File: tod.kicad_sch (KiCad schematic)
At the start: 65 parts, among them J1 2xMVE252, J2 MV133, J3 2xMVE252, J4 MV133, Q1 BC856B, Q2 BC817, Q3 BC856B, Q4 BC817, Q5 BC856, Q6 BC817, Q7 BC856, Q8 BC817, U1 PC817, U2 PC817, U3 PC817, U4 PC817

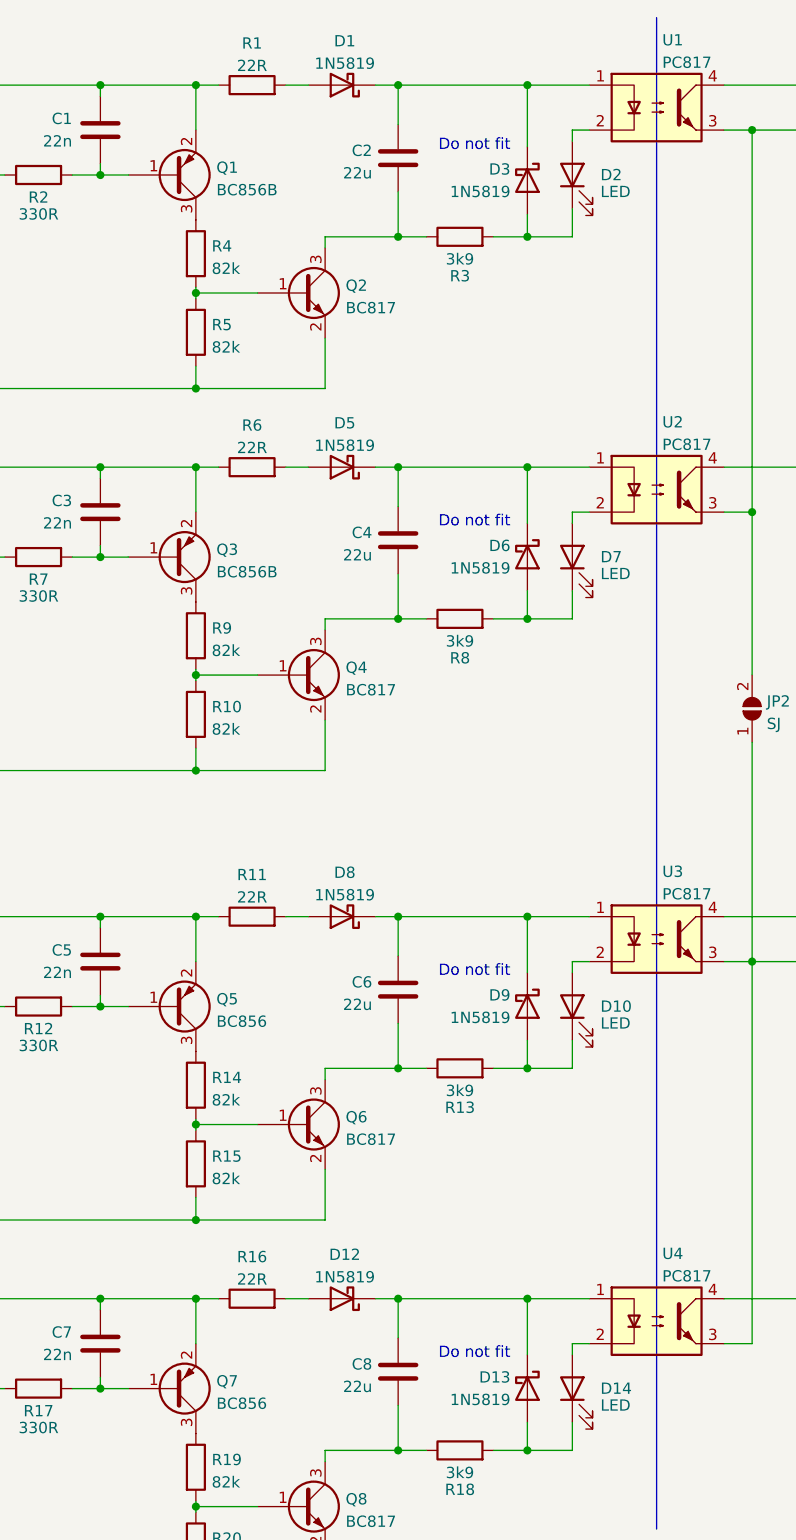
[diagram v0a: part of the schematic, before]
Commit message: Use electrolytic capacitors for 22uF C.
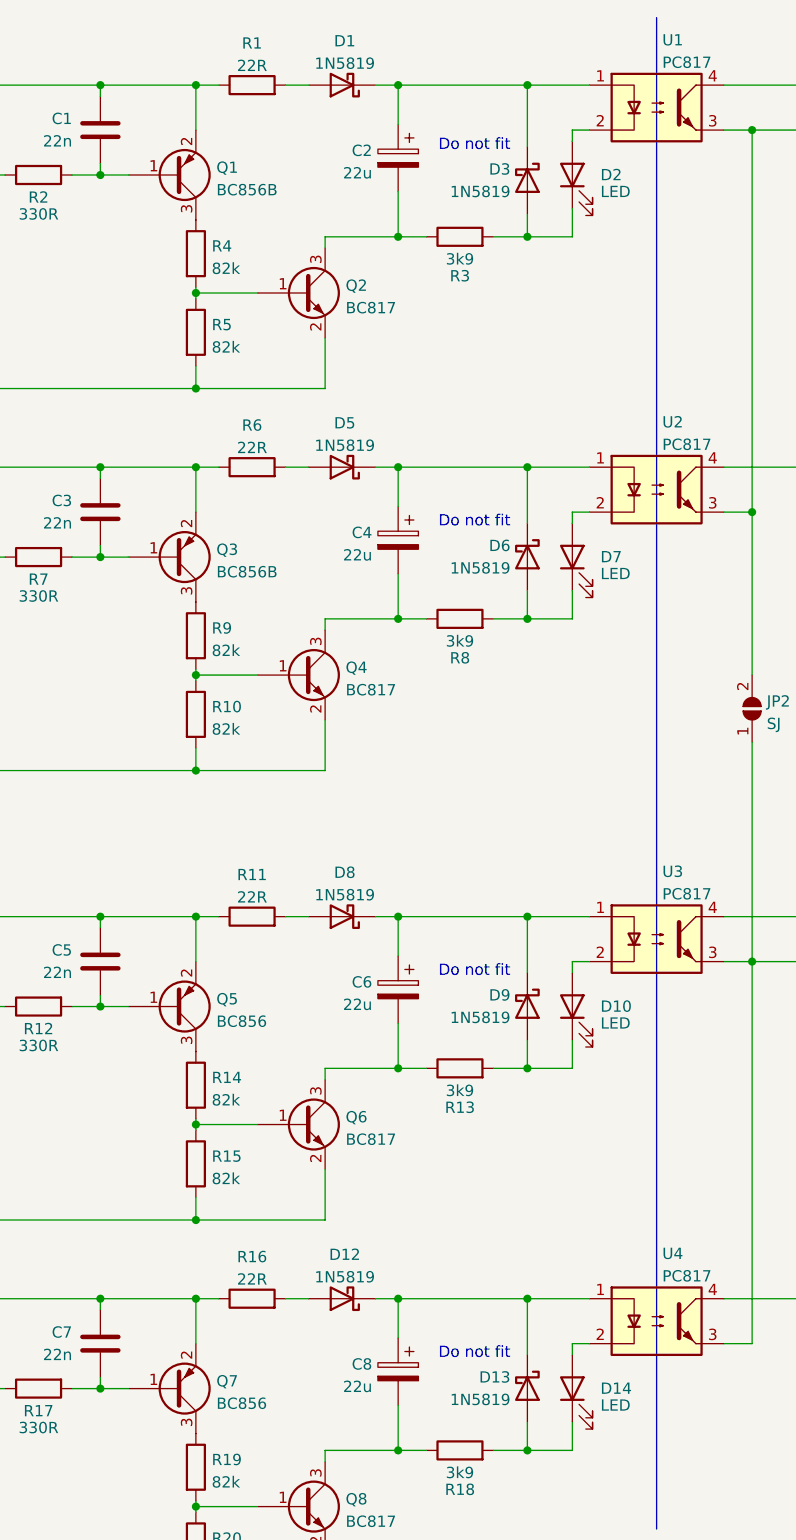
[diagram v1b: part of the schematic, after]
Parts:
- C2, C4, C6, C8: footprint Capacitor_SMD:C_0805_2012Metric_Pad1.18x1.45mm_HandSolder -> Capacitor_THT:CP_Radial_D5.0mm_P2.00mm; symbol Device:C -> Device:C_Polarized
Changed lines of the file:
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@@
   (title_block
     (title "DCC Track Occupancy Detector")
-    (date "2023-03-15")
-    (rev "1.2")
+    (date "2023-04-20")
+    (rev "1.3")
     (company "Model Railroader Club Brno I – KMŽ Brno I – https://kmz-brno.cz/")
     (comment 1 "Jan Horáček")
@@
     (pin "2")
   )
-  (symbol (lib_id "Device:C") (at 116.84 123.825 0) (mirror y) (unit 1)
+  (symbol (lib_id "Device:C_Polarized") (at 116.84 123.825 0) (mirror y) (unit 1)
     (in_bom yes) (on_board yes)
     (property "Reference" "C6" (id 0) (at 113.919 122.9903 0)
@@
       (effects (font (size 1.27 1.27)) (justify left))
     )
-    (property "Footprint" "Capacitor_SMD:C_0805_2012Metric_Pad1.18x1.45mm_HandSolder" (id 2) (at 115.8748 127.635 0)
+    (property "Footprint" "Capacitor_THT:CP_Radial_D5.0mm_P2.00mm" (id 2) (at 115.8748 127.635 0)
       (effects (font (size 1.27 1.27)) hide)
     )
@@
   (symbol (lib_id "Graphic:Logo_Open_Hardware_Small") (at 275.082 157.988 0) (unit 1)
     (in_bom yes) (on_board yes) (fields_autoplaced)
-    (property "Reference" "#LOGO?" (id 0) (at 275.082 151.003 0)
+    (property "Reference" "#LOGO1" (id 0) (at 275.082 151.003 0)
       (effects (font (size 1.27 1.27)) hide)
     )
@@
     (pin "3")
   )
-  (symbol (lib_id "Device:C") (at 116.84 167.005 0) (mirror y) (unit 1)
+  (symbol (lib_id "Device:C_Polarized") (at 116.84 167.005 0) (mirror y) (unit 1)
     (in_bom yes) (on_board yes)
     (property "Reference" "C8" (id 0) (at 113.919 166.1703 0)
@@
       (effects (font (size 1.27 1.27)) (justify left))
     )
-    (property "Footprint" "Capacitor_SMD:C_0805_2012Metric_Pad1.18x1.45mm_HandSolder" (id 2) (at 115.8748 170.815 0)
+    (property "Footprint" "Capacitor_THT:CP_Radial_D5.0mm_P2.00mm" (id 2) (at 115.8748 170.815 0)
       (effects (font (size 1.27 1.27)) hide)
     )
@@
     (pin "2")
   )
-  (symbol (lib_id "Device:C") (at 116.84 29.845 0) (mirror y) (unit 1)
+  (symbol (lib_id "Device:C_Polarized") (at 116.84 29.845 0) (mirror y) (unit 1)
     (in_bom yes) (on_board yes)
     (property "Reference" "C2" (id 0) (at 113.919 29.0103 0)
@@
       (effects (font (size 1.27 1.27)) (justify left))
     )
-    (property "Footprint" "Capacitor_SMD:C_0805_2012Metric_Pad1.18x1.45mm_HandSolder" (id 2) (at 115.8748 33.655 0)
+    (property "Footprint" "Capacitor_THT:CP_Radial_D5.0mm_P2.00mm" (id 2) (at 115.8748 33.655 0)
       (effects (font (size 1.27 1.27)) hide)
     )
@@
     (pin "2")
   )
-  (symbol (lib_id "Device:C") (at 116.84 73.025 0) (mirror y) (unit 1)
+  (symbol (lib_id "Device:C_Polarized") (at 116.84 73.025 0) (mirror y) (unit 1)
     (in_bom yes) (on_board yes)
     (property "Reference" "C4" (id 0) (at 113.919 72.1903 0)
@@
       (effects (font (size 1.27 1.27)) (justify left))
     )
-    (property "Footprint" "Capacitor_SMD:C_0805_2012Metric_Pad1.18x1.45mm_HandSolder" (id 2) (at 115.8748 76.835 0)
+    (property "Footprint" "Capacitor_THT:CP_Radial_D5.0mm_P2.00mm" (id 2) (at 115.8748 76.835 0)
       (effects (font (size 1.27 1.27)) hide)
     )
@@
   (symbol_instances
     (path "/361cc21e-47c7-4d2d-b684-c4ecf46e1791"
-      (reference "#LOGO?") (unit 1) (value "Logo_Open_Hardware_Small") (footprint "")
+      (reference "#LOGO1") (unit 1) (value "Logo_Open_Hardware_Small") (footprint "")
     )
     (path "/949e12d6-32f4-4bfa-9bdc-0a2dc68d9702"
@@
     )
     (path "/f24975cc-4930-4961-83d7-50e6801259b2"
-      (reference "C2") (unit 1) (value "22u") (footprint "Capacitor_SMD:C_0805_2012Metric_Pad1.18x1.45mm_HandSolder")
+      (reference "C2") (unit 1) (value "22u") (footprint "Capacitor_THT:CP_Radial_D5.0mm_P2.00mm")
     )
     (path "/cf8791af-62ca-417b-8de7-a76480cc2bf0"
@@
     )
     (path "/f24b77e6-aed2-4227-9685-969f1b823e6a"
-      (reference "C4") (unit 1) (value "22u") (footprint "Capacitor_SMD:C_0805_2012Metric_Pad1.18x1.45mm_HandSolder")
+      (reference "C4") (unit 1) (value "22u") (footprint "Capacitor_THT:CP_Radial_D5.0mm_P2.00mm")
     )
     (path "/0f6c05c2-d577-42fd-b418-e8c7300aab1b"
@@
     )
     (path "/0c944ec7-adc8-4223-8932-ae3fe235f03d"
-      (reference "C6") (unit 1) (value "22u") (footprint "Capacitor_SMD:C_0805_2012Metric_Pad1.18x1.45mm_HandSolder")
+      (reference "C6") (unit 1) (value "22u") (footprint "Capacitor_THT:CP_Radial_D5.0mm_P2.00mm")
     )
     (path "/f69ed3e7-e220-450f-b8ee-329eafed9527"
@@
     )
     (path "/60d53221-7944-40f6-8481-695fcfdc611f"
-      (reference "C8") (unit 1) (value "22u") (footprint "Capacitor_SMD:C_0805_2012Metric_Pad1.18x1.45mm_HandSolder")
+      (reference "C8") (unit 1) (value "22u") (footprint "Capacitor_THT:CP_Radial_D5.0mm_P2.00mm")
     )
     (path "/c44effb3-d30d-40f7-b485-7312d44f90b9"

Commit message: New capacitors: add JLCPCB_IGNORE.
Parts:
- C2, C4, C6, C8: JLCPCB_IGNORE (none) -> true; LCSC C45783 -> (none)
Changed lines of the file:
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@@
       (effects (font (size 1.27 1.27)) hide)
     )
-    (property "LCSC" "C45783" (id 4) (at 116.84 123.825 0)
+    (property "LCSC" "" (id 4) (at 116.84 123.825 0)
+      (effects (font (size 1.27 1.27)) hide)
+    )
+    (property "JLCPCB_IGNORE" "true" (id 5) (at 116.84 123.825 0)
       (effects (font (size 1.27 1.27)) hide)
     )
@@
       (effects (font (size 1.27 1.27)) hide)
     )
-    (property "LCSC" "C45783" (id 4) (at 116.84 167.005 0)
+    (property "LCSC" "" (id 4) (at 116.84 167.005 0)
+      (effects (font (size 1.27 1.27)) hide)
+    )
+    (property "JLCPCB_IGNORE" "true" (id 5) (at 116.84 167.005 0)
       (effects (font (size 1.27 1.27)) hide)
     )
@@
       (effects (font (size 1.27 1.27)) hide)
     )
-    (property "LCSC" "C45783" (id 4) (at 116.84 29.845 0)
+    (property "LCSC" "" (id 4) (at 116.84 29.845 0)
+      (effects (font (size 1.27 1.27)) hide)
+    )
+    (property "JLCPCB_IGNORE" "true" (id 5) (at 116.84 29.845 0)
       (effects (font (size 1.27 1.27)) hide)
     )
@@
       (effects (font (size 1.27 1.27)) hide)
     )
-    (property "LCSC" "C45783" (id 4) (at 116.84 73.025 0)
-      (effects (font (size 1.27 1.27)) hide)
-    )
+    (property "LCSC" "" (id 4) (at 116.84 73.025 0)
+      (effects (font (size 1.27 1.27)) hide)
+    )
+    (property "JLCPCB_IGNORE" "true" (id 5) (at 116.84 73.025 0)
+      (effects (font (size 1.27 1.27)) hide)
+    )

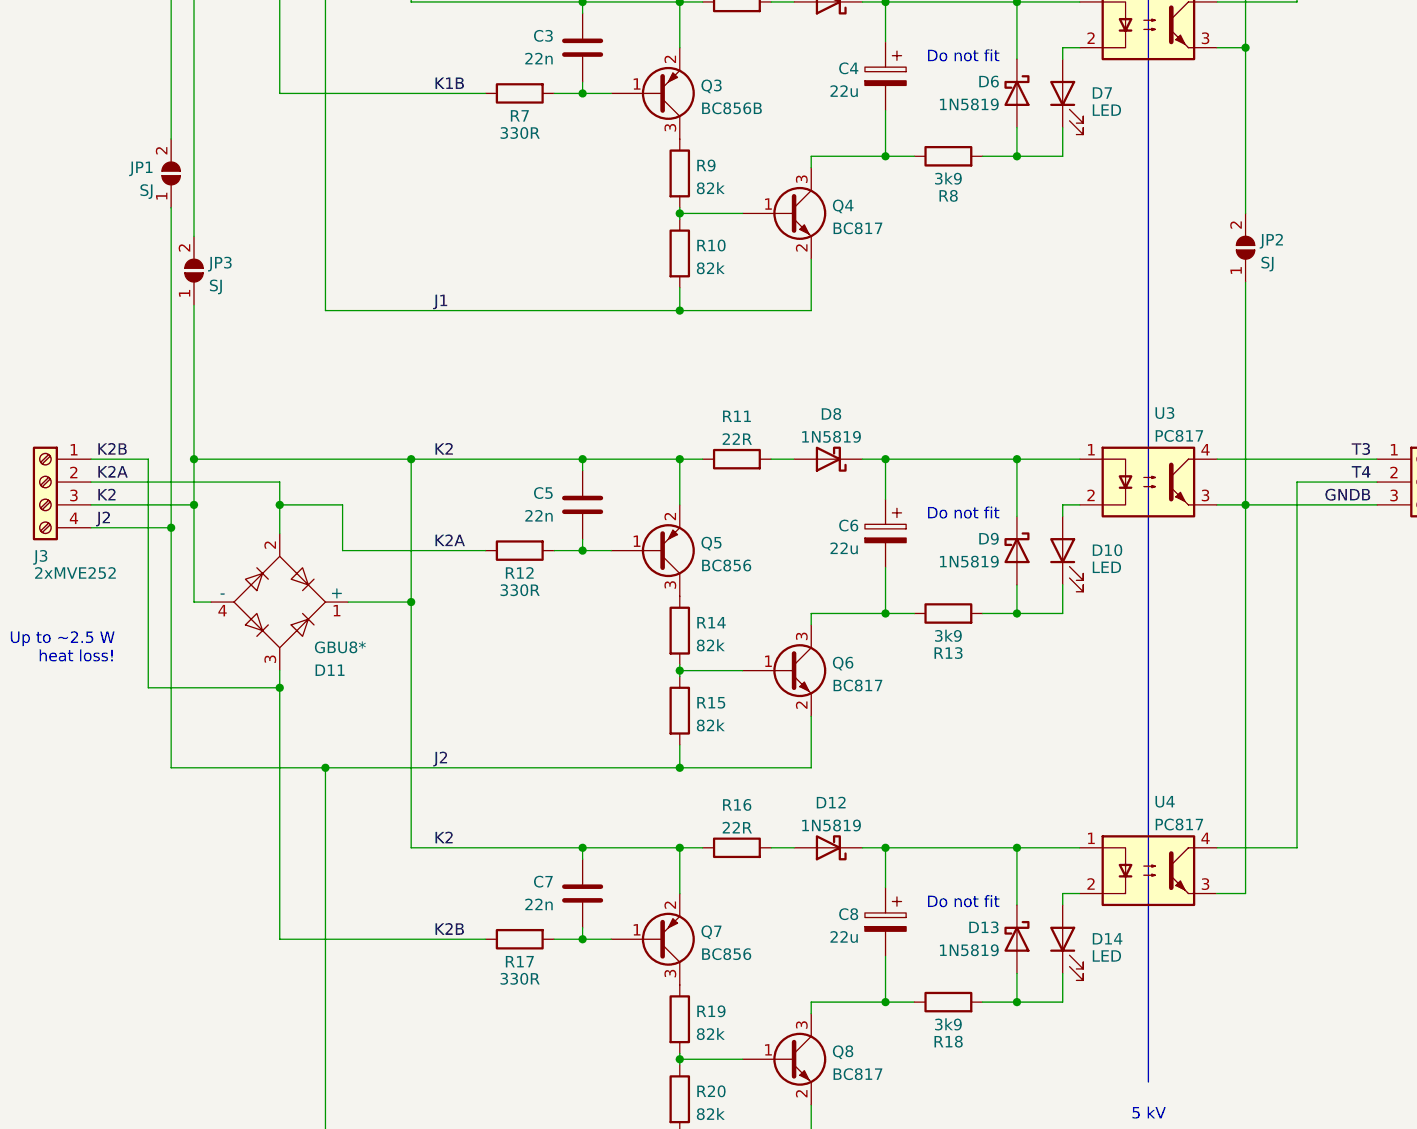
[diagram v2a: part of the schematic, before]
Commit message: Migrate to KiCad 7, add missing 'B' to all BC856 transistors.
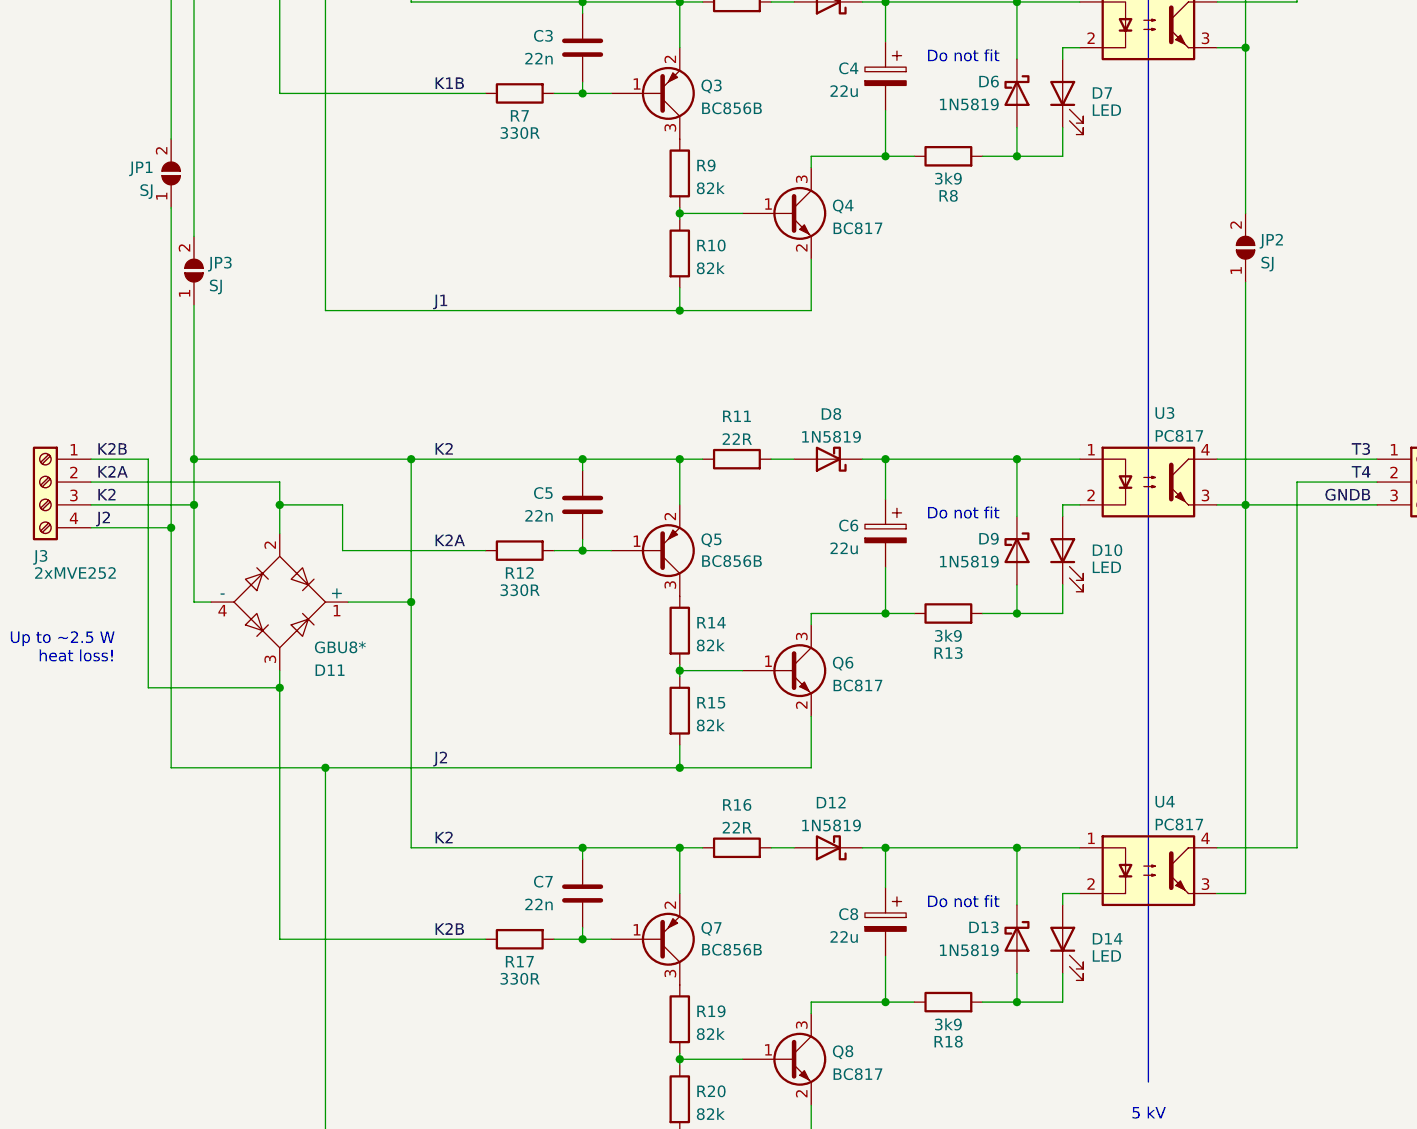
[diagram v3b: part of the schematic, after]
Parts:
- Q5, Q7: value BC856 -> BC856B
